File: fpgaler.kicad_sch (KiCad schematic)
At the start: 53 parts, among them J1 USB_C_Receptacle_USB2.0, J2 JST, J3 Conn_01x08_MountingPin, J4 FTDI_RST, SW1 RotaryEncoder_Switch, SW2 RotaryEncoder_Switch, SW3 K1, SW4 K2, SW5 PROGRAMN, SW6 K3, SW7 FPGA GSRN, SW8 K4

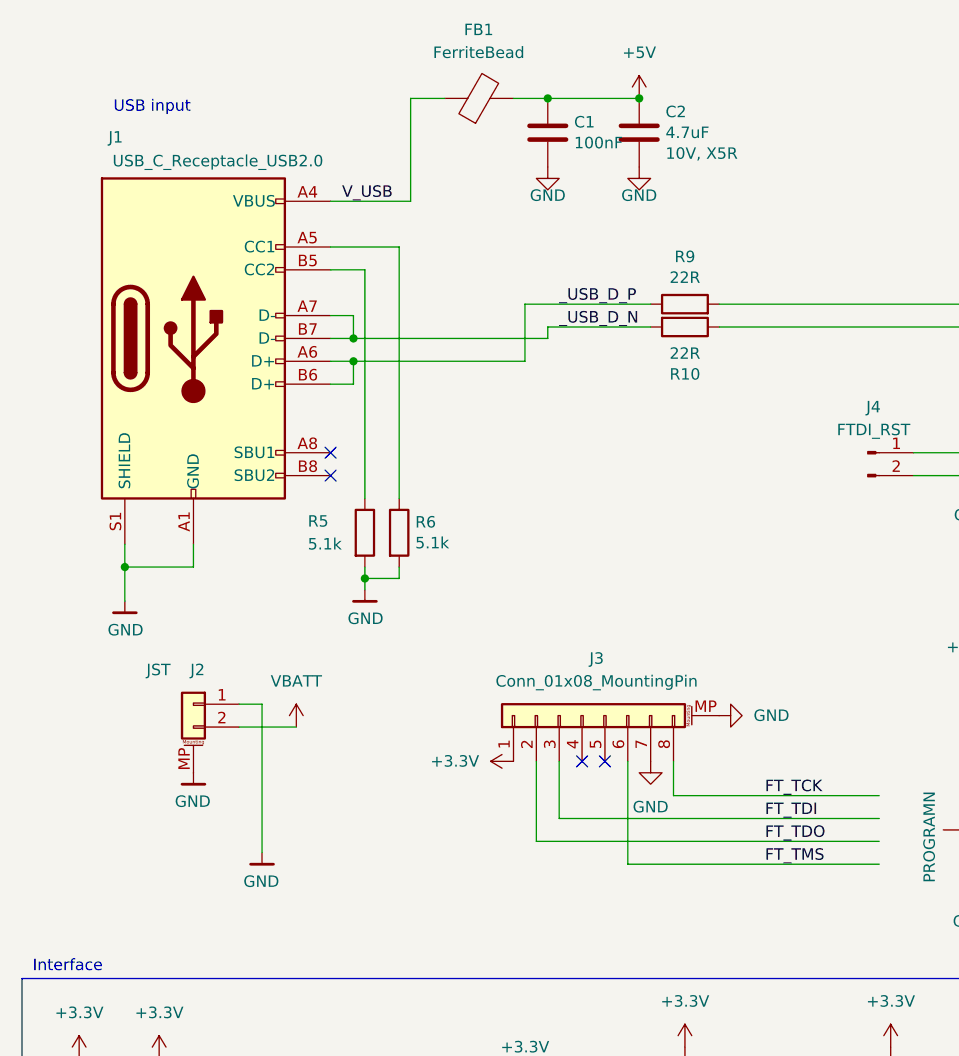
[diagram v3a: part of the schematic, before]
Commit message: Assign jlcpcb pn. Fix footprint assign, uniform resistor value for battery charger
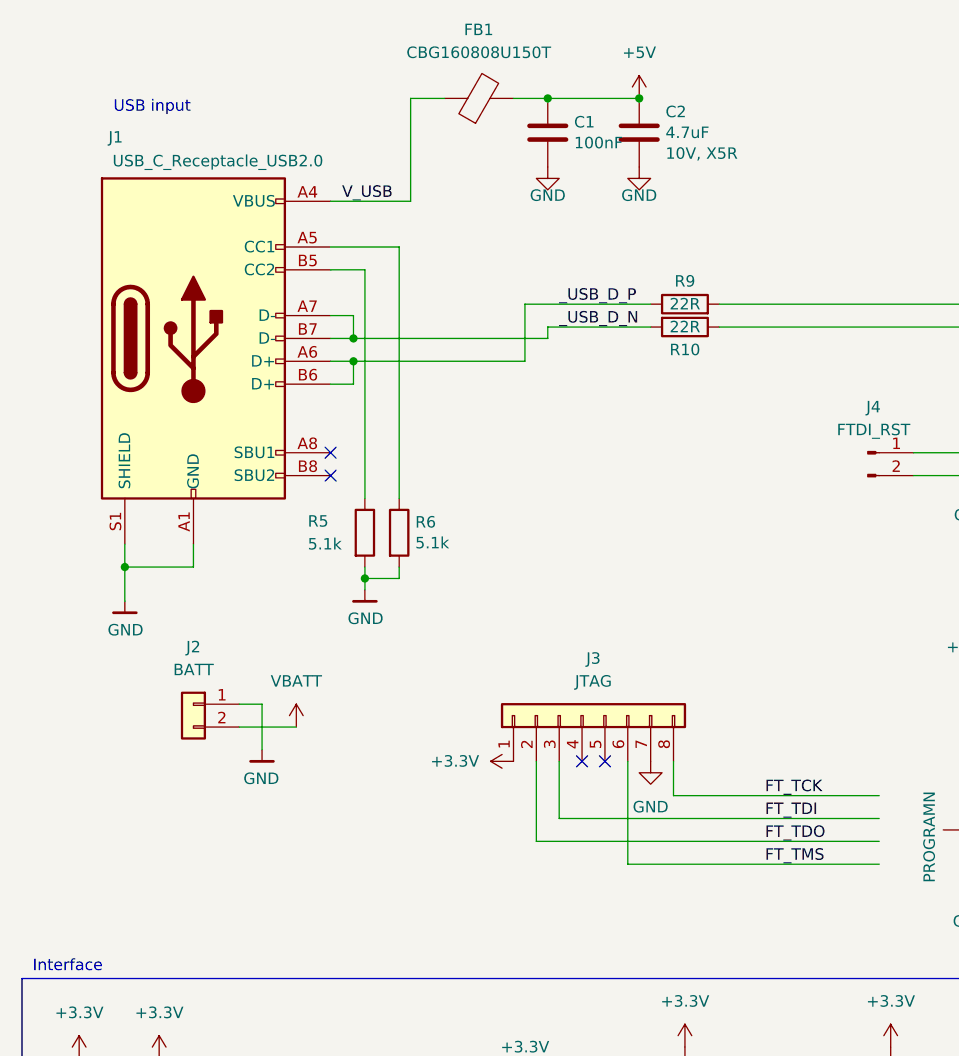
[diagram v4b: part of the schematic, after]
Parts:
- removed J2: JST, gkl_conn:JST_PH_B2B-PH-SM4-TB_1x02-1MP_P2.00mm_Vertical, symbol Connector_Generic_MountingPin:Conn_01x02_MountingPin
- removed J3: Conn_01x08_MountingPin, Connector_PinHeader_2.54mm:PinHeader_1x08_P2.54mm_Vertical, symbol Connector_Generic_MountingPin:Conn_01x08_MountingPin
- added J2: BATT, Connector_JST:JST_PH_S2B-PH-K_1x02_P2.00mm_Horizontal, symbol Connector_Generic:Conn_01x02
- added J3: JTAG, Connector_PinHeader_2.54mm:PinHeader_1x08_P2.54mm_Vertical, symbol Connector_Generic:Conn_01x08
- FB1: value FerriteBead -> CBG160808U150T; footprint (none) -> Inductor_SMD:L_0603_1608Metric
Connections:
- net +3.3V: now also J3.1 (Pin_1)
- net FT_TCK: now also J3.8 (Pin_8)
- net FT_TDI: now also J3.3 (Pin_3)
- net FT_TDO: now also J3.2 (Pin_2)
- net FT_TMS: now also J3.6 (Pin_6)
- net GND: now also J2.1 (Pin_1), J3.7 (Pin_7)
- net VBATT: now also J2.2 (Pin_2)

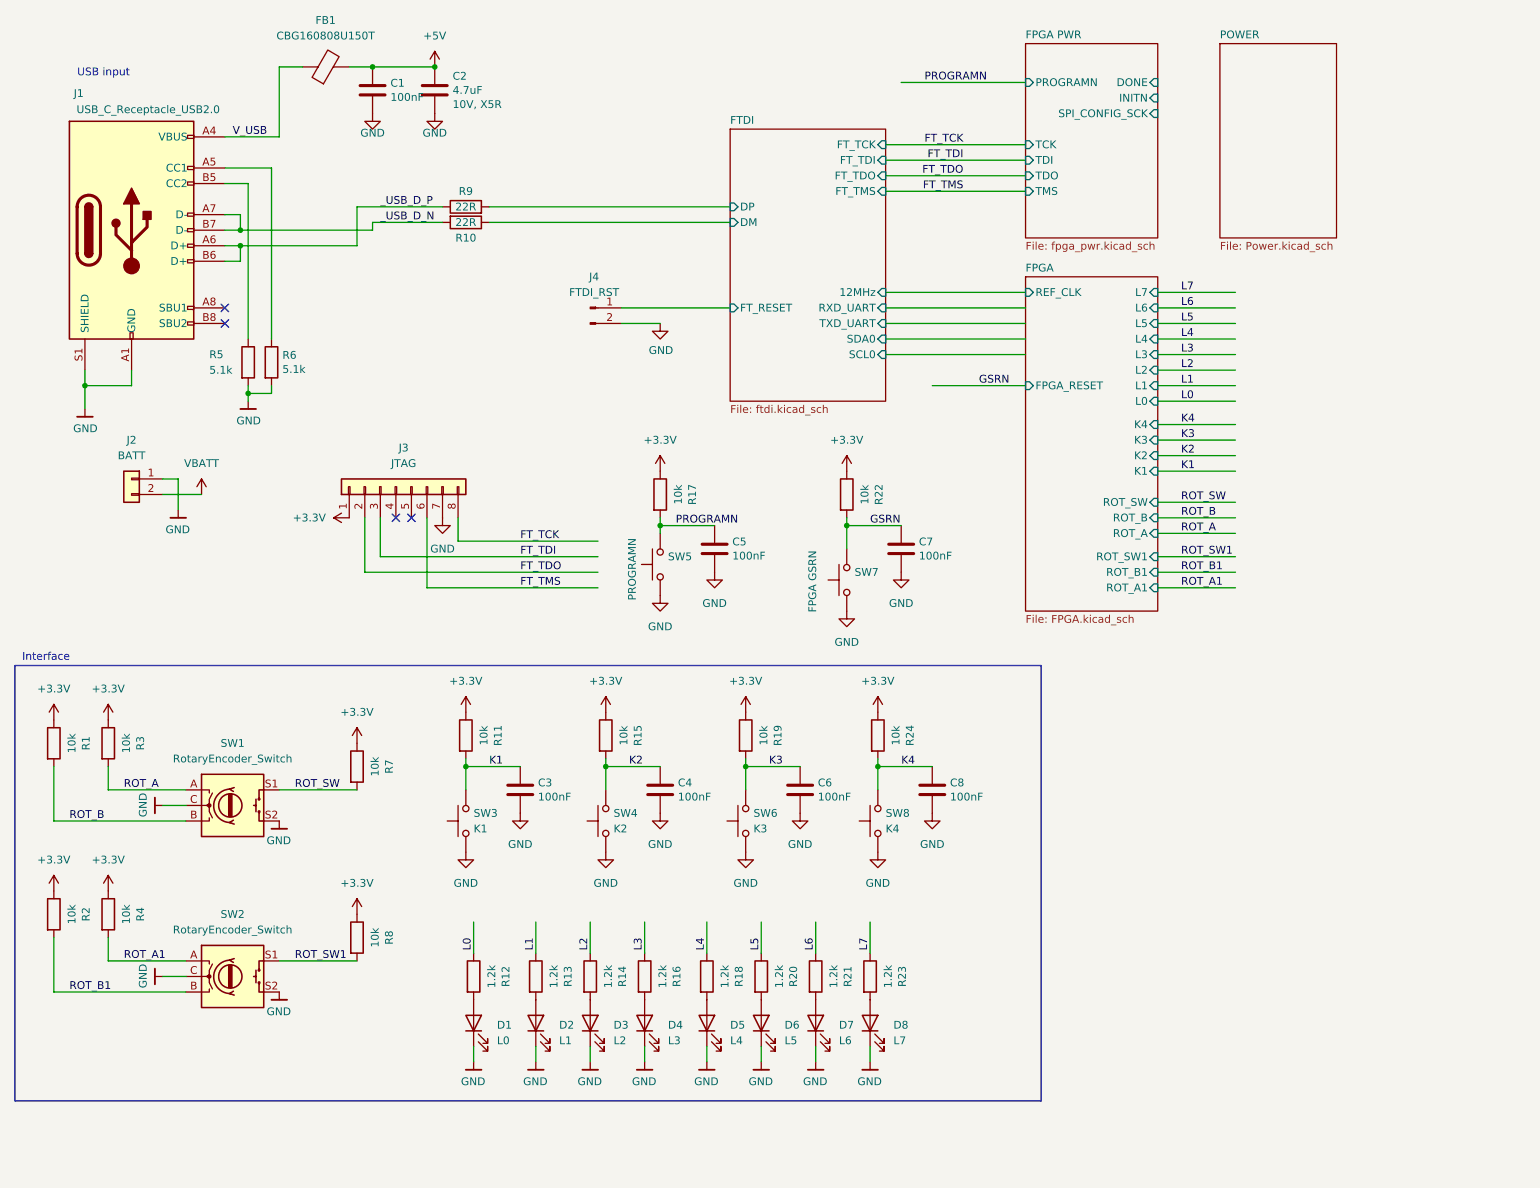
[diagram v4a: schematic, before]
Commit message: Add sram and oscillator 27MHz
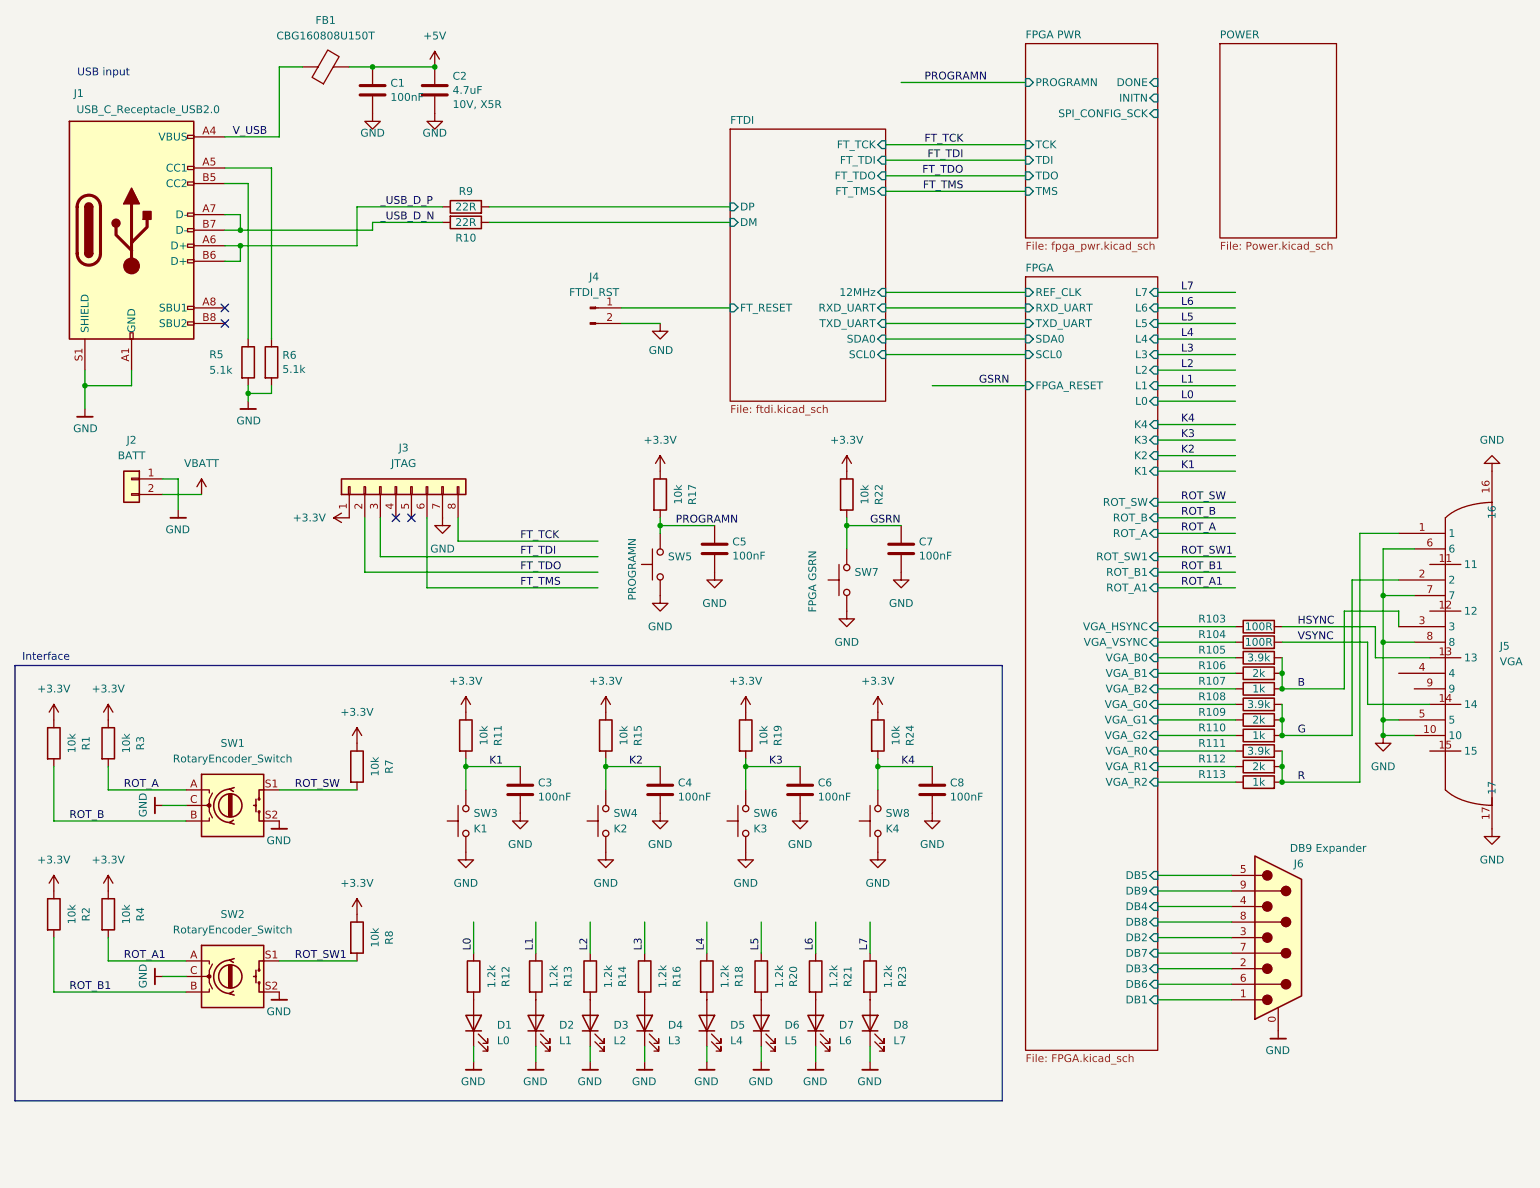
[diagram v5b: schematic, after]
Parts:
- added J5: VGA, EasyEDA_Lib:DSUB-TH_HYC06-HDR15B-060, symbol EasyEDA_Lib:HYC06-HDR15B-060
- added J6: DB9 Expander, Connector_Dsub:DSUB-9_Pins_Horizontal_P2.77x2.84mm_EdgePinOffset4.94mm_Housed_MountingHolesOffset4.94mm, symbol Connector:DE9_Pins_MountingHoles
- added R103, R104: 100R, Resistor_SMD:R_0603_1608Metric, symbol Device:R
- added R105, R108, R111: 3.9k, Resistor_SMD:R_0603_1608Metric, symbol Device:R
- added R106, R109, R112: 2k, Resistor_SMD:R_0603_1608Metric, symbol Device:R
- added R107, R110, R113: 1k, Resistor_SMD:R_0603_1608Metric, symbol Device:R
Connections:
- net GND: now also J5.10, J5.16, J5.17, J5.5, J5.6, J5.7, J5.8, J6.0 (PAD)
- new net B: J5.3, R105.2, R106.2, R107.2
- new net FPGA/DB1: J6.1
- new net FPGA/DB2: J6.3
- new net FPGA/DB3: J6.2
- new net FPGA/DB4: J6.4
- new net FPGA/DB5: J6.5
- new net FPGA/DB6: J6.6
- new net FPGA/DB7: J6.7
- new net FPGA/DB8: J6.8
- new net FPGA/DB9: J6.9
- new net FPGA/VGA_B0: R105.1
- new net FPGA/VGA_B1: R106.1
- new net FPGA/VGA_B2: R107.1
- new net FPGA/VGA_G0: R108.1
- new net FPGA/VGA_G1: R109.1
- new net FPGA/VGA_G2: R110.1
- new net FPGA/VGA_HSYNC: R103.1
- new net FPGA/VGA_R0: R111.1
- new net FPGA/VGA_R1: R112.1
- new net FPGA/VGA_R2: R113.1
- new net FPGA/VGA_VSYNC: R104.1
- new net G: J5.2, R108.2, R109.2, R110.2
- new net HSYNC: J5.13, R103.2
- new net R: J5.1, R111.2, R112.2, R113.2
- new net VSYNC: J5.14, R104.2
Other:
- sheet FPGA ports: added DB1, DB2, DB3, DB4, DB5, DB6, DB7, DB8, DB9, RXD_UART, SCL0, SDA0, TXD_UART, VGA_B0, VGA_B1, VGA_B2, VGA_G0, VGA_G1, VGA_G2, VGA_HSYNC, VGA_R0, VGA_R1, VGA_R2, VGA_VSYNC; removed none

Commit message: routing sram
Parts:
- J2: LCSC (none) -> C173752
- J5: JLC_3DModel_Q (none) -> 8413562495e247b795cb16dbfce09eda; JLC_3D_Size (none) -> 30.8 14.8
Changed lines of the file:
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@@
+			)
+		)
+		(property "LCSC" "C173752"
+			(at 34.29 92.71 0)
+			(effects
+				(font
+					(size 1.27 1.27)
+				)
+				(hide yes)
 			)
 		)
@@
 			(at 251.46 119.38 0)
 			(effects
+				(font
+					(size 1.27 1.27)
+				)
+				(hide yes)
+			)
+		)
+		(property "JLC_3DModel_Q" "8413562495e247b795cb16dbfce09eda"
+			(at 251.46 119.38 0)
+			(effects
+				(font
+					(size 1.27 1.27)
+				)
+				(hide yes)
+			)
+		)
+		(property "JLC_3D_Size" "30.8 14.8"
+			(at 251.46 119.38 0)
+			(effects

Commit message: Routing sram
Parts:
- R10, R9: footprint Resistor_SMD:R_0603_1608Metric -> Resistor_SMD:R_01005_0402Metric_Pad0.57x0.30mm_HandSolder
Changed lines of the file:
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@@
 			)
 		)
-		(property "Footprint" "Resistor_SMD:R_0603_1608Metric"
+		(property "Footprint" "Resistor_SMD:R_01005_0402Metric_Pad0.57x0.30mm_HandSolder"
 			(at 88.9 50.038 90)
 			(effects
@@
 			)
 		)
-		(property "Footprint" "Resistor_SMD:R_0603_1608Metric"
+		(property "Footprint" "Resistor_SMD:R_01005_0402Metric_Pad0.57x0.30mm_HandSolder"
 			(at 88.9 49.022 90)
 			(effects

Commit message: Complete SRAM, and routing VGA
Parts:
- R10, R9: footprint Resistor_SMD:R_01005_0402Metric_Pad0.57x0.30mm_HandSolder -> Resistor_SMD:R_0402_1005Metric_Pad0.72x0.64mm_HandSolder
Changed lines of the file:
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@@
 			)
 		)
-		(property "Footprint" "Resistor_SMD:R_01005_0402Metric_Pad0.57x0.30mm_HandSolder"
+		(property "Footprint" "Resistor_SMD:R_0402_1005Metric_Pad0.72x0.64mm_HandSolder"
 			(at 88.9 50.038 90)
 			(effects
@@
 			)
 		)
-		(property "Footprint" "Resistor_SMD:R_01005_0402Metric_Pad0.57x0.30mm_HandSolder"
+		(property "Footprint" "Resistor_SMD:R_0402_1005Metric_Pad0.72x0.64mm_HandSolder"
 			(at 88.9 49.022 90)
 			(effects
